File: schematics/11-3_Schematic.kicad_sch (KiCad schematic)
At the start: 7 parts, among them U1 SSD1306 OLED 0.96in

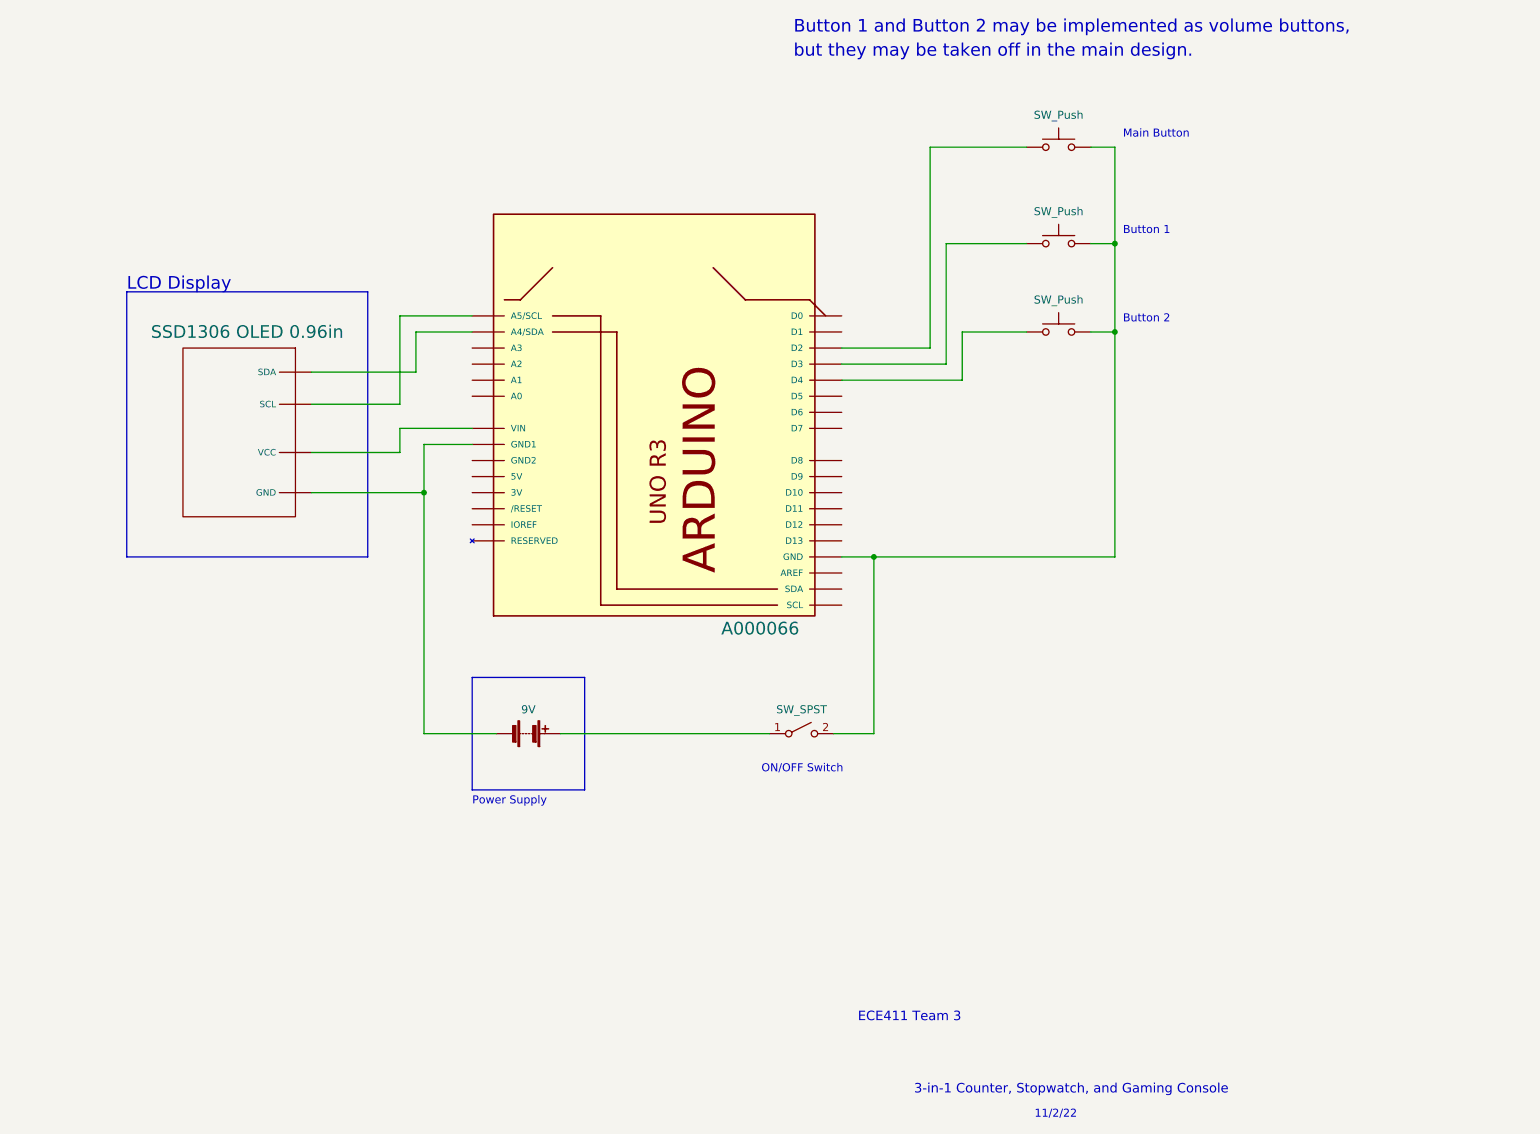
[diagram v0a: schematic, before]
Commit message: corrected gnd wire on right side
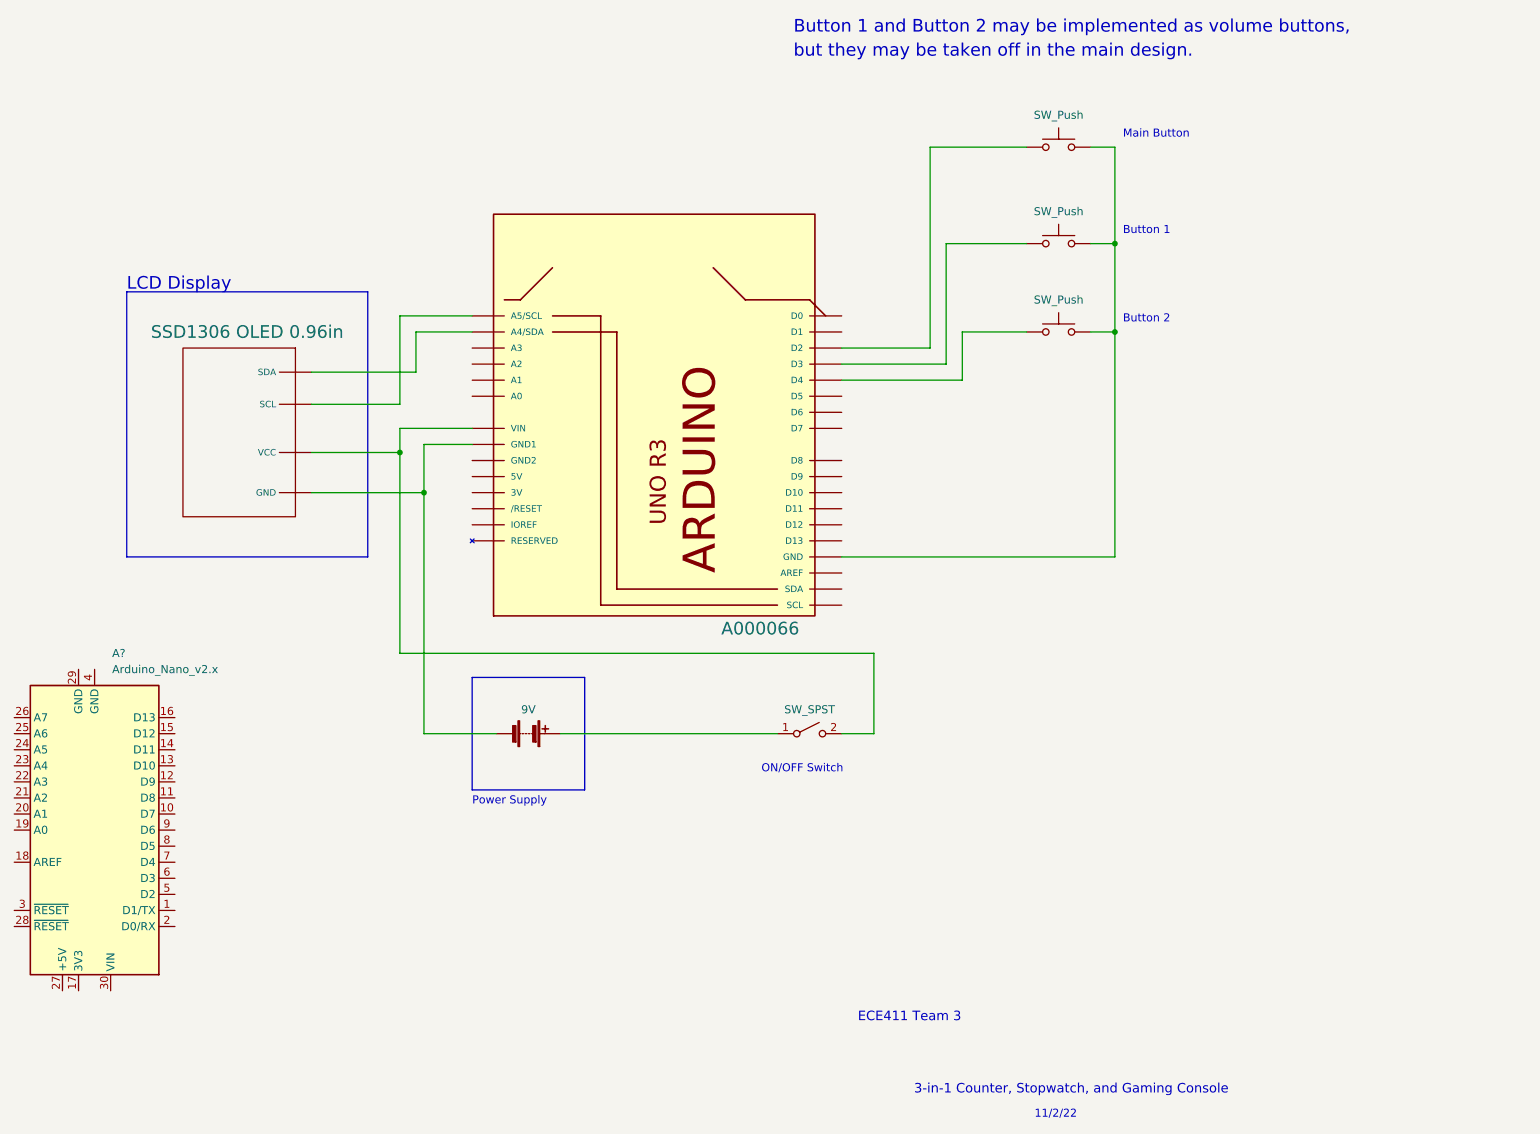
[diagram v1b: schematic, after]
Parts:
- added A?: Arduino_Nano_v2.x, Module:Arduino_Nano, symbol MCU_Module:Arduino_Nano_v2.x
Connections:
- net at ModelA66.GND, R13-507-5-X1.2, R13-507-5-X2.2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: no longer KCD1-1-101-ON-OFF-X1.2 (B)
- net at ModelA66.VIN, U1. (VCC): now also KCD1-1-101-ON-OFF-X1.2 (B)
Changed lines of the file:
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@@
 (kicad_sch (version 20211123) (generator eeschema)
   (paper "A4")
+  (junction (at 106.68 88.9) (diameter 0) (color 0 0 0 0)
+  )
   (junction (at 110.49 95.25) (diameter 0) (color 0 0 0 0)
   )
   (junction (at 219.71 55.88) (diameter 0) (color 0 0 0 0)
   )
-  (junction (at 181.61 105.41) (diameter 0) (color 0 0 0 0)
-  )
   (junction (at 219.71 69.85) (diameter 0) (color 0 0 0 0)
   )
@@
     (stroke (width 0) (type default) (color 0 0 0 0))
   )
-  (wire (pts (xy 175.26 133.35) (xy 181.61 133.35))
+  (wire (pts (xy 106.68 120.65) (xy 181.61 120.65))
+    (stroke (width 0) (type default) (color 0 0 0 0))
+  )
+  (wire (pts (xy 176.53 133.35) (xy 181.61 133.35))
     (stroke (width 0) (type default) (color 0 0 0 0))
   )
@@
     (stroke (width 0) (type default) (color 0 0 0 0))
   )
-  (wire (pts (xy 181.61 105.41) (xy 176.53 105.41))
+  (wire (pts (xy 176.53 105.41) (xy 219.71 105.41))
     (stroke (width 0) (type default) (color 0 0 0 0))
   )
@@
     (stroke (width 0) (type default) (color 0 0 0 0))
   )
+  (wire (pts (xy 132.08 133.35) (xy 166.37 133.35))
+    (stroke (width 0) (type default) (color 0 0 0 0))
+  )
   (wire (pts (xy 110.49 95.25) (xy 110.49 87.63))
     (stroke (width 0) (type default) (color 0 0 0 0))
@@
     (stroke (width 0) (type default) (color 0 0 0 0))
   )
+  (wire (pts (xy 181.61 120.65) (xy 181.61 133.35))
+    (stroke (width 0) (type default) (color 0 0 0 0))
+  )
   (wire (pts (xy 92.71 95.25) (xy 110.49 95.25))
     (stroke (width 0) (type default) (color 0 0 0 0))
@@
     (stroke (width 0) (type default) (color 0 0 0 0))
   )
-  (wire (pts (xy 132.08 133.35) (xy 165.1 133.35))
+  (wire (pts (xy 106.68 88.9) (xy 106.68 120.65))
     (stroke (width 0) (type default) (color 0 0 0 0))
   )
@@
   )
   (wire (pts (xy 176.53 72.39) (xy 190.5 72.39))
-    (stroke (width 0) (type default) (color 0 0 0 0))
-  )
-  (wire (pts (xy 219.71 105.41) (xy 181.61 105.41))
-    (stroke (width 0) (type default) (color 0 0 0 0))
-  )
-  (wire (pts (xy 181.61 133.35) (xy 181.61 105.41))
     (stroke (width 0) (type default) (color 0 0 0 0))
   )
@@
     (pin "2")
   )
+  (symbol (lib_id "MCU_Module:Arduino_Nano_v2.x") (at 58.42 148.59 180) (unit 1)
+    (in_bom yes) (on_board yes) (fields_autoplaced)
+    (property "Reference" "A?" (id 0) (at 61.1887 120.65 0)
+      (effects (font (size 1.27 1.27)) (justify right))
+    )
+    (property "Value" "Arduino_Nano_v2.x" (id 1) (at 61.1887 123.19 0)
+      (effects (font (size 1.27 1.27)) (justify right))
+    )
+    (property "Footprint" "Module:Arduino_Nano" (id 2) (at 58.42 148.59 0)
+      (effects (font (size 1.27 1.27) italic) hide)
+    )
+    (property "Datasheet" "https://www.arduino.cc/en/uploads/Main/ArduinoNanoManual23.pdf" (id 3) (at 58.42 148.59 0)
+      (effects (font (size 1.27 1.27)) hide)
+    )
+    (pin "1")
+    (pin "10")
+    (pin "11")
+    (pin "12")
+    (pin "13")
+    (pin "14")
+    (pin "15")
+    (pin "16")
+    (pin "17")
+    (pin "18")
+    (pin "19")
+    (pin "2")
+    (pin "20")
+    (pin "21")
+    (pin "22")
+    (pin "23")
+    (pin "24")
+    (pin "25")
+    (pin "26")
+    (pin "27")
+    (pin "28")
+    (pin "29")
+    (pin "3")
+    (pin "30")
+    (pin "4")
+    (pin "5")
+    (pin "6")
+    (pin "7")
+    (pin "8")
+    (pin "9")
+  )
   (symbol (lib_id "Switch:SW_Push") (at 210.82 69.85 0) (unit 1)
     (in_bom yes) (on_board yes) (fields_autoplaced)
@@
     (pin "2")
   )
-  (symbol (lib_id "Switch:SW_SPST") (at 170.18 133.35 0) (unit 1)
-    (in_bom yes) (on_board yes) (fields_autoplaced)
-    (property "Reference" "KCD1-1-101-ON-OFF-X1" (id 0) (at 170.18 127 0)
-      (effects (font (size 1.27 1.27)) hide)
-    )
-    (property "Value" "SW_SPST" (id 1) (at 170.18 129.54 0))
-    (property "Footprint" "" (id 2) (at 170.18 133.35 0)
-      (effects (font (size 1.27 1.27)) hide)
-    )
-    (property "Datasheet" "~" (id 3) (at 170.18 133.35 0)
+  (symbol (lib_id "Switch:SW_SPST") (at 171.45 133.35 0) (unit 1)
+    (in_bom yes) (on_board yes) (fields_autoplaced)
+    (property "Reference" "KCD1-1-101-ON-OFF-X1" (id 0) (at 171.45 127 0)
+      (effects (font (size 1.27 1.27)) hide)
+    )
+    (property "Value" "SW_SPST" (id 1) (at 171.45 129.54 0))
+    (property "Footprint" "" (id 2) (at 171.45 133.35 0)
+      (effects (font (size 1.27 1.27)) hide)
+    )
+    (property "Datasheet" "~" (id 3) (at 171.45 133.35 0)
       (effects (font (size 1.27 1.27)) hide)
     )
@@
   )
   (symbol_instances
+    (path "/33bc4c2f-62f1-4e72-a766-bd152cc212d9"
+      (reference "A?") (unit 1) (value "Arduino_Nano_v2.x") (footprint "Module:Arduino_Nano")
+    )
     (path "/911ffd39-dab6-4aa2-8103-741b4c41b721"
       (reference "Battery1") (unit 1) (value "9V") (footprint "")

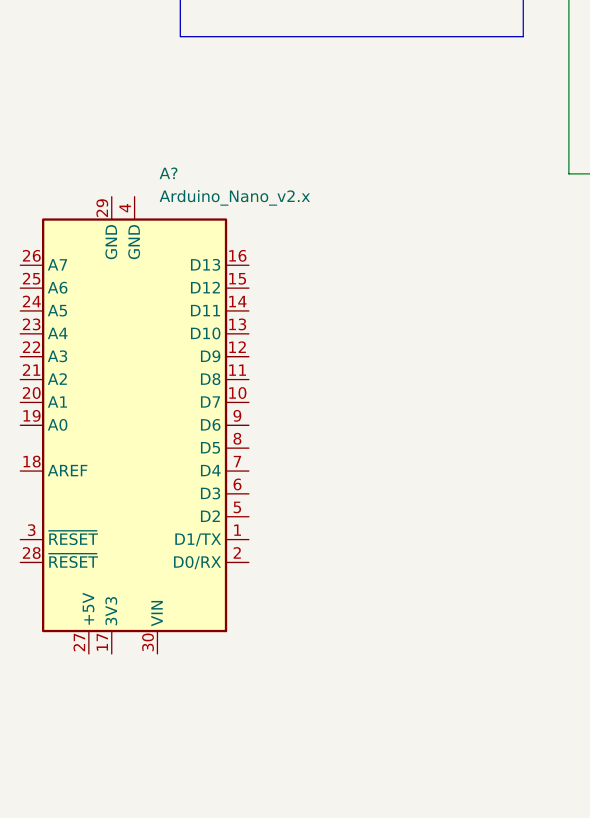
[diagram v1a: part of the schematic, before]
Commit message: corrected wire going to gnd on right side
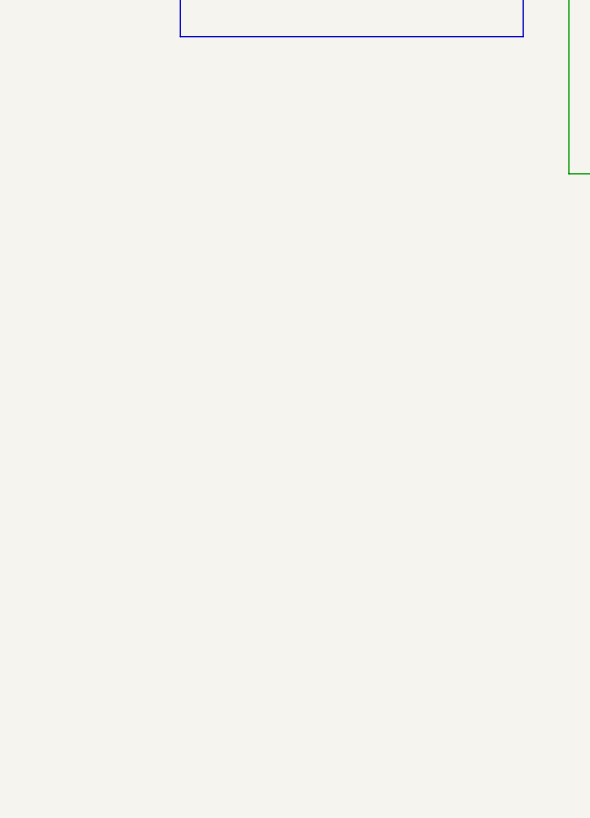
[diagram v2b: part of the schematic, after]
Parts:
- removed A?: Arduino_Nano_v2.x, Module:Arduino_Nano, symbol MCU_Module:Arduino_Nano_v2.x
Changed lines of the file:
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@@
     (pin "2")
-  )
-  (symbol (lib_id "MCU_Module:Arduino_Nano_v2.x") (at 58.42 148.59 180) (unit 1)
-    (in_bom yes) (on_board yes) (fields_autoplaced)
-    (property "Reference" "A?" (id 0) (at 61.1887 120.65 0)
-      (effects (font (size 1.27 1.27)) (justify right))
-    )
-    (property "Value" "Arduino_Nano_v2.x" (id 1) (at 61.1887 123.19 0)
-      (effects (font (size 1.27 1.27)) (justify right))
-    )
-    (property "Footprint" "Module:Arduino_Nano" (id 2) (at 58.42 148.59 0)
-      (effects (font (size 1.27 1.27) italic) hide)
-    )
-    (property "Datasheet" "https://www.arduino.cc/en/uploads/Main/ArduinoNanoManual23.pdf" (id 3) (at 58.42 148.59 0)
-      (effects (font (size 1.27 1.27)) hide)
-    )
-    (pin "1")
-    (pin "10")
-    (pin "11")
-    (pin "12")
-    (pin "13")
-    (pin "14")
-    (pin "15")
-    (pin "16")
-    (pin "17")
-    (pin "18")
-    (pin "19")
-    (pin "2")
-    (pin "20")
-    (pin "21")
-    (pin "22")
-    (pin "23")
-    (pin "24")
-    (pin "25")
-    (pin "26")
-    (pin "27")
-    (pin "28")
-    (pin "29")
-    (pin "3")
-    (pin "30")
-    (pin "4")
-    (pin "5")
-    (pin "6")
-    (pin "7")
-    (pin "8")
-    (pin "9")
   )
   (symbol (lib_id "Switch:SW_Push") (at 210.82 69.85 0) (unit 1)
@@
   )
   (symbol_instances
-    (path "/33bc4c2f-62f1-4e72-a766-bd152cc212d9"
-      (reference "A?") (unit 1) (value "Arduino_Nano_v2.x") (footprint "Module:Arduino_Nano")
-    )
     (path "/911ffd39-dab6-4aa2-8103-741b4c41b721"
       (reference "Battery1") (unit 1) (value "9V") (footprint "")
